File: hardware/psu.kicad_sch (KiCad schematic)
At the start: 59 parts, among them IC301 TLV61220DBVT, J301 Barrel_Jack_Switch, J302 Conn_01x03, Q301 CSD87503Q3E, Q302 CSD87503Q3E, Q303 Q_NMOS, U301 TPS63020DSJR, U302 BQ25798RQMR

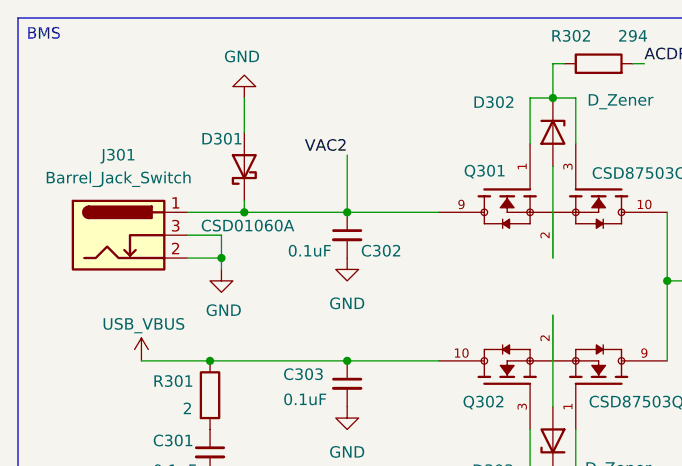
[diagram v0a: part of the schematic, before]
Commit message: updated ESD/Inductor footprints
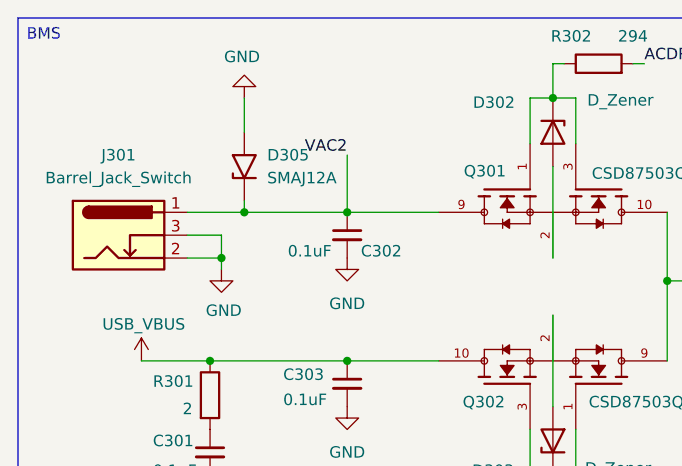
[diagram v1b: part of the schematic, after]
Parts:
- removed D301: CSD01060A, Diode_SMD:D_SOD-123, symbol Diode:CSD01060A
- added D305: SMAJ12A, Diode_SMD:D_SMA, symbol Diode:SMAJ12A
- L301: footprint Inductor_SMD:L_0805_2012Metric -> Inductor_SMD:L_Wuerth_MAPI-4020
- L302: footprint Inductor_SMD:L_0805_2012Metric -> Inductor_SMD:L_Bourns_SRP7028A_7.3x6.6mm
- L303: footprint Inductor_SMD:L_0805_2012Metric -> Inductor_SMD:L_1210_3225Metric
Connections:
- net GND: now also D305.2 (A2)
- net VAC2: now also D305.1 (A1)
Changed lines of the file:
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@@
 	)
 	(symbol
+		(lib_id "Diode:SMAJ12A")
+		(at 40.64 30.48 90)
+		(unit 1)
+		(exclude_from_sim no)
+		(in_bom yes)
+		(on_board yes)
+		(dnp no)
+		(fields_autoplaced yes)
+		(property "Reference" "D305"
+			(at 43.18 29.2099 90)
+			(effects
+				(font
+					(size 1.27 1.27)
+				)
+				(justify right)
+			)
+		)
+		(property "Value" "SMAJ12A"
+			(at 43.18 31.7499 90)
+			(effects
+				(font
+					(size 1.27 1.27)
+				)
+				(justify right)
+			)
+		)
+		(property "Footprint" "Diode_SMD:D_SMA"
+			(at 45.72 30.48 0)
+			(effects
+				(font
+					(size 1.27 1.27)
+				)
+				(hide yes)
+			)
+		)
+		(property "Datasheet" "https://www.littelfuse.com/media?resourcetype=datasheets&itemid=75e32973-b177-4ee3-a0ff-cedaf1abdb93&filename=smaj-datasheet"
+			(at 40.64 31.75 0)
+			(effects
+				(font
+					(size 1.27 1.27)
+				)
+				(hide yes)
+			)
+		)
+		(property "Description" "400W unidirectional Transient Voltage Suppressor, 12.0Vr, SMA(DO-214AC)"
+			(at 40.64 30.48 0)
+			(effects
+				(font
+					(size 1.27 1.27)
+				)
+				(hide yes)
+			)
+		)
+		(pin "1"
+		)
+		(pin "2"
+		)
+		(instances
+			(project ""
+				(path "/8f5928e8-0fc1-4443-a20f-3bfeb956761e/09dae378-4d12-4dca-bc21-c216f94ec21f"
+					(reference "D305")
+					(unit 1)
+				)
+			)
+		)
+	)
+	(symbol
 		(lib_id "power:GND")
 		(at 226.06 111.76 0)
@@
 			)
 		)
-		(property "Footprint" "Inductor_SMD:L_0805_2012Metric"
+		(property "Footprint" "Inductor_SMD:L_1210_3225Metric"
 			(at 208.28 133.35 0)
 			(effects
@@
 			)
 		)
-		(property "Footprint" "Inductor_SMD:L_0805_2012Metric"
+		(property "Footprint" "Inductor_SMD:L_Bourns_SRP7028A_7.3x6.6mm"
 			(at 119.38 68.58 0)
 			(effects
@@
 			)
 		)
-		(property "Footprint" "Inductor_SMD:L_0805_2012Metric"
+		(property "Footprint" "Inductor_SMD:L_Wuerth_MAPI-4020"
 			(at 113.03 158.75 0)
 			(effects
@@
 					(unit 1)
 				)
-			)
-		)
-	)
-	(symbol
-		(lib_id "Diode:CSD01060A")
-		(at 40.64 30.48 90)
-		(unit 1)
-		(exclude_from_sim no)
-		(in_bom yes)
-		(on_board yes)
-		(dnp no)
-		(property "Reference" "D301"
-			(at 35.814 27.432 90)
-			(effects
-				(font
-					(size 1.27 1.27)
-				)
-				(justify right)
-			)
-		)
-		(property "Value" "CSD01060A"
-			(at 35.814 37.084 90)
-			(effects
-				(font
-					(size 1.27 1.27)
-				)
-				(justify right)
-			)
-		)
-		(property "Footprint" "Diode_SMD:D_SOD-123"
-			(at 45.085 30.48 0)
-			(effects
-				(font
-					(size 1.27 1.27)
-				)
-				(hide yes)
-			)
-		)
-		(property "Datasheet" "https://www.wolfspeed.com/media/downloads/87/CSD01060.pdf"
-			(at 40.64 30.48 0)
-			(effects
-				(font
-					(size 1.27 1.27)
-				)
-				(hide yes)
-			)
-		)
-		(property "Description" "600V, 1A, SiC Schottky Diode, TO-220"
-			(at 40.64 30.48 0)
-			(effects
-				(font
-					(size 1.27 1.27)
-				)
-				(hide yes)
-			)
-		)
-		(pin "2"
-		)
-		(pin "1"
-		)
-		(instances
-			(project "Senior_Design"
-				(path "/8f5928e8-0fc1-4443-a20f-3bfeb956761e/09dae378-4d12-4dca-bc21-c216f94ec21f"
-					(reference "D301")
-					(unit 1)
-				)

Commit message: pcb_update_1232
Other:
- moved on the sheet: R311
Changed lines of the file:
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@@
 	(symbol
 		(lib_id "Device:R")
-		(at 214.63 36.83 180)
+		(at 214.63 36.83 0)
+		(mirror x)
 		(unit 1)
 		(exclude_from_sim no)
@@
 		(dnp no)
 		(property "Reference" "R311"
-			(at 220.218 33.274 0)
+			(at 209.042 33.274 0)
 			(effects
 				(font
@@
 		)
 		(property "Value" "100"
-			(at 219.202 40.64 0)
+			(at 210.058 40.64 0)
 			(effects
 				(font
@@
 		)
 		(property "Footprint" "Resistor_SMD:R_0805_2012Metric"
-			(at 216.408 36.83 90)
+			(at 212.852 36.83 90)
 			(effects
 				(font

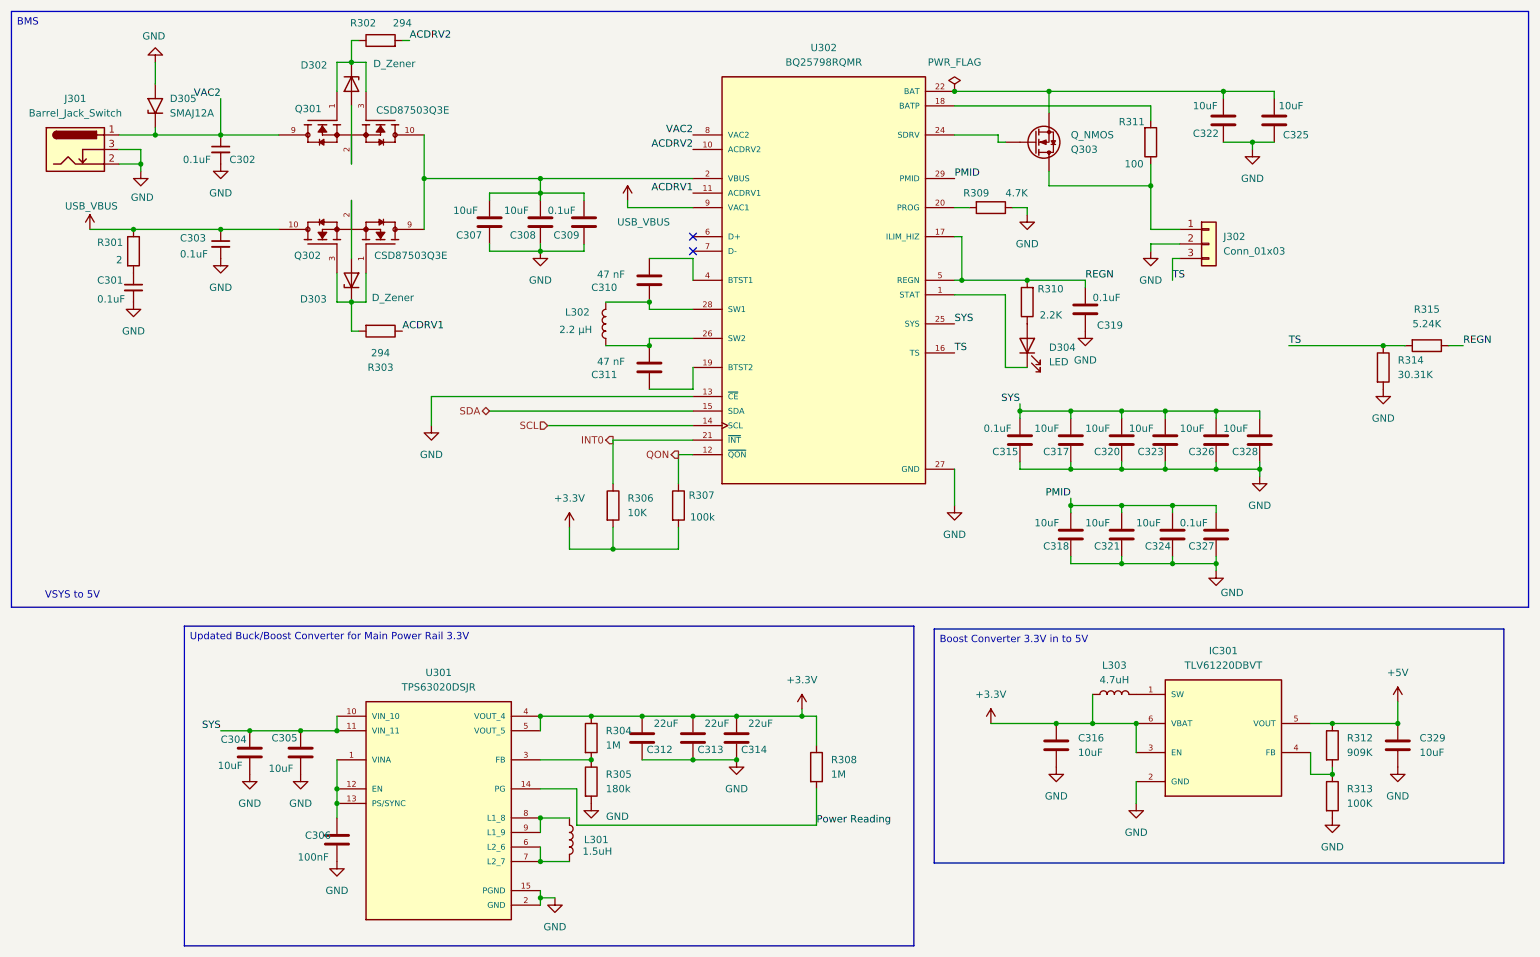
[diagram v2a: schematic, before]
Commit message: updated footprints
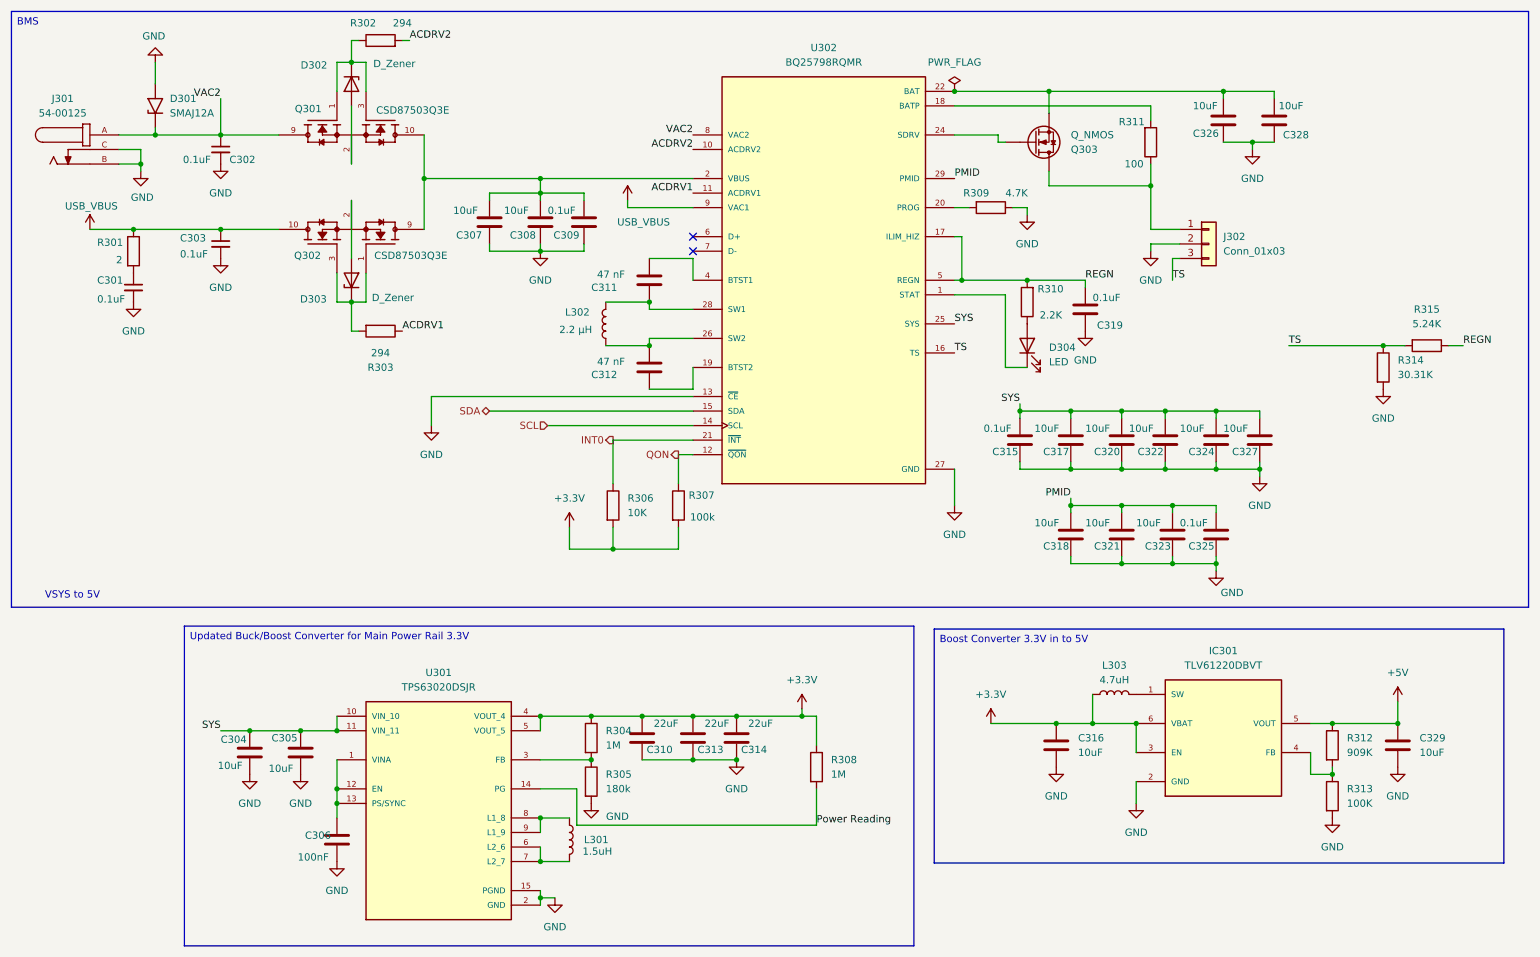
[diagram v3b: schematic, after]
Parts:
- removed J301: Barrel_Jack_Switch, Connector_BarrelJack:BarrelJack_Wuerth_694102107102_1.0x3.9mm, symbol Connector:Barrel_Jack_Switch
- added J301: 54-00125, pyronet_footprints:TENSILITY_54-00125, symbol pyronet_symbols:54-00125
- renumbered C312 to C310, C310 to C311, C311 to C312, C323 to C322, C324 to C323, C326 to C324, C327 to C325, C322 to C326, C328 to C327, C325 to C328, D305 to D301
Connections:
- net GND: now also J301.B, J301.C
- net VAC2: now also J301.A
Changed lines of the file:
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@@
 		(on_board yes)
 		(dnp no)
-		(property "Reference" "C312"
+		(property "Reference" "C310"
 			(at 131.064 143.002 0)
 			(effects
@@
 			(project "Senior_Design"
 				(path "/8f5928e8-0fc1-4443-a20f-3bfeb956761e/09dae378-4d12-4dca-bc21-c216f94ec21f"
-					(reference "C312")
+					(reference "C310")
 					(unit 1)
 				)
@@
 		(on_board yes)
 		(dnp no)
-		(property "Reference" "C322"
+		(property "Reference" "C326"
 			(at 221.996 35.306 0)
 			(effects
@@
 			(project "Senior_Design"
 				(path "/8f5928e8-0fc1-4443-a20f-3bfeb956761e/09dae378-4d12-4dca-bc21-c216f94ec21f"
-					(reference "C322")
+					(reference "C326")
 					(unit 1)
 				)
@@
 		(on_board yes)
 		(dnp no)
-		(property "Reference" "C326"
+		(property "Reference" "C324"
 			(at 221.234 90.932 0)
 			(effects
@@
 			(project "Senior_Design"
 				(path "/8f5928e8-0fc1-4443-a20f-3bfeb956761e/09dae378-4d12-4dca-bc21-c216f94ec21f"
-					(reference "C326")
+					(reference "C324")
 					(unit 1)
 				)
@@
 		(on_board yes)
 		(dnp no)
-		(property "Reference" "C323"
+		(property "Reference" "C322"
 			(at 212.344 90.932 0)
 			(effects
@@
 			(project "Senior_Design"
 				(path "/8f5928e8-0fc1-4443-a20f-3bfeb956761e/09dae378-4d12-4dca-bc21-c216f94ec21f"
-					(reference "C323")
+					(reference "C322")
 					(unit 1)
 				)
@@
 		(dnp no)
 		(fields_autoplaced yes)
-		(property "Reference" "D305"
+		(property "Reference" "D301"
 			(at 43.18 29.2099 90)
 			(effects
@@
 			(project ""
 				(path "/8f5928e8-0fc1-4443-a20f-3bfeb956761e/09dae378-4d12-4dca-bc21-c216f94ec21f"
-					(reference "D305")
+					(reference "D301")
 					(unit 1)
 				)
@@
 		(on_board yes)
 		(dnp no)
-		(property "Reference" "#PWR0326"
+		(property "Reference" "#PWR0325"
 			(at 226.06 118.11 0)
 			(effects
@@
 			(project "Senior_Design"
 				(path "/8f5928e8-0fc1-4443-a20f-3bfeb956761e/09dae378-4d12-4dca-bc21-c216f94ec21f"
-					(reference "#PWR0326")
+					(reference "#PWR0325")
 					(unit 1)
 				)
@@
 		(on_board yes)
 		(dnp no)
-		(property "Reference" "C325"
+		(property "Reference" "C328"
 			(at 237.744 35.56 0)
 			(effects
@@
 			(project "Senior_Design"
 				(path "/8f5928e8-0fc1-4443-a20f-3bfeb956761e/09dae378-4d12-4dca-bc21-c216f94ec21f"
-					(reference "C325")
+					(reference "C328")
 					(unit 1)
 				)
@@
 	)
 	(symbol
+		(lib_id "pyronet_symbols:54-00125")
+		(at 29.21 38.1 0)
+		(unit 1)
+		(exclude_from_sim no)
+		(in_bom yes)
+		(on_board yes)
+		(dnp no)
+		(fields_autoplaced yes)
+		(property "Reference" "J301"
+			(at 24.4503 29.21 0)
+			(effects
+				(font
+					(size 1.27 1.27)
+				)
+			)
+		)
+		(property "Value" "54-00125"
+			(at 24.4503 31.75 0)
+			(effects
+				(font
+					(size 1.27 1.27)
+				)
+			)
+		)
+		(property "Footprint" "pyronet_footprints:TENSILITY_54-00125"
+			(at 29.21 38.1 0)
+			(effects
+				(font
+					(size 1.27 1.27)
+				)
+				(justify bottom)
+				(hide yes)
+			)
+		)
+		(property "Datasheet" ""
+			(at 29.21 38.1 0)
+			(effects
+				(font
+					(size 1.27 1.27)
+				)
+				(hide yes)
+			)
+		)
+		(property "Description" ""
+			(at 29.21 38.1 0)
+			(effects
+				(font
+					(size 1.27 1.27)
+				)
+				(hide yes)
+			)
+		)
+		(property "DigiKey_Part_Number" "839-54-00125-ND"
+			(at 29.21 38.1 0)
+			(effects
+				(font
+					(size 1.27 1.27)
+				)
+				(justify bottom)
+				(hide yes)
+			)
+		)
+		(property "SnapEDA_Link" "https://www.snapeda.com/parts/54-00125/Tensility/view-part/?ref=snap"
+			(at 29.21 38.1 0)
+			(effects
+				(font
+					(size 1.27 1.27)
+				)
+				(justify bottom)
+				(hide yes)
+			)
+		)
+		(property "MAXIMUM_PACKAGE_HEIGHT" "5.7mm"
+			(at 29.21 38.1 0)
+			(effects
+				(font
+					(size 1.27 1.27)
+				)
+				(justify bottom)
+				(hide yes)
+			)
+		)
+		(property "Package" "None"
+			(at 29.21 38.1 0)
+			(effects
+				(font
+					(size 1.27 1.27)
+				)
+				(justify bottom)
+				(hide yes)
+			)
+		)
+		(property "Check_prices" "https://www.snapeda.com/parts/54-00125/Tensility/view-part/?ref=eda"
+			(at 29.21 38.1 0)
+			(effects
+				(font
+					(size 1.27 1.27)
+				)
+				(justify bottom)
+				(hide yes)
+			)
+		)
+		(property "STANDARD" "Manufacturer Recommendations"
+			(at 29.21 38.1 0)
+			(effects
+				(font
+					(size 1.27 1.27)
+				)
+				(justify bottom)
+				(hide yes)
+			)
+		)
+		(property "PARTREV" "A"
+			(at 29.21 38.1 0)
+			(effects
+				(font
+					(size 1.27 1.27)
+				)
+				(justify bottom)
+				(hide yes)
+			)
+		)
+		(property "MF" "Tensility International Corp"
+			(at 29.21 38.1 0)
+			(effects
+				(font
+					(size 1.27 1.27)
+				)
+				(justify bottom)
+				(hide yes)
+			)
+		)
+		(property "MP" "54-00125"
+			(at 29.21 38.1 0)
+			(effects
+				(font
+					(size 1.27 1.27)
+				)
+				(justify bottom)
+				(hide yes)
+			)
+		)
+		(property "Description_1" "Connector, dc jack 3.5x1.1 mm, PCB mount, 90 degrees, silver plated, thru hole"
+			(at 29.21 38.1 0)
+			(effects
+				(font
+					(size 1.27 1.27)
+				)
+				(justify bottom)
+				(hide yes)
+			)
+		)
+		(property "MANUFACTURER" "TENSILITY"
+			(at 29.21 38.1 0)
+			(effects
+				(font
+					(size 1.27 1.27)
+				)
+				(justify bottom)
+				(hide yes)
+			)
+		)
+		(property "SNAPEDA_PN" "54-00125"
+			(at 29.21 38.1 0)
+			(effects
+				(font
+					(size 1.27 1.27)
+				)
+				(justify bottom)
+				(hide yes)
+			)
+		)
+		(pin "C"
+		)
+		(pin "B"
+		)
+		(pin "A"
+		)
+		(instances
+			(project ""
+				(path "/8f5928e8-0fc1-4443-a20f-3bfeb956761e/09dae378-4d12-4dca-bc21-c216f94ec21f"
+					(reference "J301")
+					(unit 1)
+				)
+			)
+		)
+	)
+	(symbol
 		(lib_id "power:GND")
 		(at 246.38 154.94 0)
@@
 		(on_board yes)
 		(dnp no)
-		(property "Reference" "C311"
+		(property "Reference" "C312"
 			(at 116.84 77.47 0)
 			(effects
@@
 			(project "Senior_Design"
 				(path "/8f5928e8-0fc1-4443-a20f-3bfeb956761e/09dae378-4d12-4dca-bc21-c216f94ec21f"
-					(reference "C311")
+					(reference "C312")
 					(unit 1)
 				)
@@
 		(on_board yes)
 		(dnp no)
-		(property "Reference" "C310"
+		(property "Reference" "C311"
 			(at 116.84 62.23 0)
 			(effects
@@
 			(project "Senior_Design"
 				(path "/8f5928e8-0fc1-4443-a20f-3bfeb956761e/09dae378-4d12-4dca-bc21-c216f94ec21f"
-					(reference "C310")
+					(reference "C311")
 					(unit 1)
 				)
@@
 		(on_board yes)
 		(dnp no)
-		(property "Reference" "C324"
+		(property "Reference" "C323"
 			(at 213.614 107.442 0)
 			(effects
@@
 			(project "Senior_Design"
 				(path "/8f5928e8-0fc1-4443-a20f-3bfeb956761e/09dae378-4d12-4dca-bc21-c216f94ec21f"
-					(reference "C324")
+					(reference "C323")
 					(unit 1)
 				)
@@
 		(on_board yes)
 		(dnp no)
-		(property "Reference" "C327"
+		(property "Reference" "C325"
 			(at 221.234 107.442 0)
 			(effects
@@
 			(project "Senior_Design"
 				(path "/8f5928e8-0fc1-4443-a20f-3bfeb956761e/09dae378-4d12-4dca-bc21-c216f94ec21f"
-					(reference "C327")
+					(reference "C325")
 					(unit 1)
 				)
@@
 		(dnp no)
 		(fields_autoplaced yes)
-		(property "Reference" "#PWR0325"
+		(property "Reference" "#PWR0326"
 			(at 232.41 44.45 0)
 			(effects
@@
 			(project "Senior_Design"
 				(path "/8f5928e8-0fc1-4443-a20f-3bfeb956761e/09dae378-4d12-4dca-bc21-c216f94ec21f"
-					(reference "#PWR0325")
+					(reference "#PWR0326")
 					(unit 1)
 				)
@@
 	)
 	(symbol
-		(lib_id "Connector:Barrel_Jack_Switch")
-		(at 26.67 38.1 0)
-		(unit 1)
-		(exclude_from_sim no)
-		(in_bom yes)
-		(on_board yes)
-		(dnp no)
-		(fields_autoplaced yes)
-		(property "Reference" "J301"
-			(at 26.67 29.21 0)
-			(effects
-				(font
-					(size 1.27 1.27)
-				)
-			)
-		)
-		(property "Value" "Barrel_Jack_Switch"
-			(at 26.67 31.75 0)
-			(effects
-				(font
-					(size 1.27 1.27)
-				)
-			)
-		)
-		(property "Footprint" "Connector_BarrelJack:BarrelJack_Wuerth_694102107102_1.0x3.9mm"
-			(at 27.94 39.116 0)
-			(effects
-				(font
-					(size 1.27 1.27)
-				)
-				(hide yes)
-			)
-		)
-		(property "Datasheet" "~"
-			(at 27.94 39.116 0)
-			(effects
-				(font
-					(size 1.27 1.27)
-				)
-				(hide yes)
-			)
-		)
-		(property "Description" "DC Barrel Jack with an internal switch"
-			(at 26.67 38.1 0)
-			(effects
-				(font
-					(size 1.27 1.27)
-				)
-				(hide yes)
-			)
-		)
-		(pin "2"
-		)
-		(pin "3"
-		)
-		(pin "1"
-		)
-		(instances
-			(project "Senior_Design"
-				(path "/8f5928e8-0fc1-4443-a20f-3bfeb956761e/09dae378-4d12-4dca-bc21-c216f94ec21f"
-					(reference "J301")
-					(unit 1)
-				)
-			)
-		)
-	)
-	(symbol
 		(lib_id "Device:C")
 		(at 200.66 105.41 0)
@@
 		(on_board yes)
 		(dnp no)
-		(property "Reference" "C328"
+		(property "Reference" "C327"
 			(at 228.854 90.932 0)
 			(effects
@@
 			(project "Senior_Design"
 				(path "/8f5928e8-0fc1-4443-a20f-3bfeb956761e/09dae378-4d12-4dca-bc21-c216f94ec21f"
-					(reference "C328")
+					(reference "C327")
 					(unit 1)
 				)
